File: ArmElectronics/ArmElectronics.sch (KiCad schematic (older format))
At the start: 90 parts, among them J1 Raspberry_Pi_2_3, J10 AH1815 Breakout, J11 AH1815 Breakout, J12 AH1815 Breakout, J13 AH1815 Breakout, J14 AH1815 Breakout, J15 AH1815 Breakout, J16 AH1815 Breakout, J17 AH1815 Breakout, J18 AH1815 Breakout, J19 AH1815 Breakout, J2 12V In, J20 AH1815 Breakout, J21 AH1815 Breakout, J3 RasPi Power Out, J4 Batt In, J5 Batt Out, J6 BNO055 QWIIC Conn, J7 Conn_01x14, J8 Encoder Breakout, J9 1792245, U1 Teensy4.1, U10 PA-09, U11 74LVC1G97, U12 74LVC1G97, U13 74LVC1G97, U14 74LVC1G97, U15 74LVC1G97, U16 74LVC1G97, U18 MAX11601, U2 Pololu_2857, U3 Pololu_2851, U4 Pololu_3730, U5 TB9051FTG, U6 TB9051FTG, U7 TB9051FTG, U8 PA-09, U9 PA-09

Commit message: reannotated schematic
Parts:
- renumbered C7 to C1, C1 to C2, C2 to C3, C3 to C4, C4 to C5, C5 to C6, C6 to C7, J18 to J17, J19 to J18, J20 to J19, J7 to J2, J21 to J20, J9 to J21, J8 to J3, J3 to J4, J2 to J5, J4 to J6, J5 to J7, J6 to J8, J17 to J9, R31 to R1, R40 to R10, R41 to R11, R25 to R12, R26 to R13, R4 to R14, R5 to R15, R6 to R16, R10 to R17, R11 to R18, R12 to R19, R32 to R2, R1 to R20, R2 to R21, R27 to R22, R28 to R23, R3 to R24, R7 to R25, R13 to R26, R14 to R27, R15 to R28, R16 to R29, R33 to R3, R17 to R30, R18 to R31, R29 to R32, R30 to R33, R8 to R34, R9 to R35, R19 to R36, R20 to R37, R21 to R38, R22 to R39, R34 to R4, R23 to R40, R24 to R41, R35 to R5, R36 to R6, R38 to R7, R39 to R8, R37 to R9, U9 to U10, U10 to U11, U11 to U12, U12 to U13, U13 to U14, U14 to U15, U15 to U16, U16 to U17, U18 to U3, U3 to U4, U4 to U5, U5 to U6, U6 to U7, U7 to U8, U8 to U9
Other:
- moved on the sheet: J10, J11, J12, J13, J14, J15, J16, J17, J18, J19, J20, J9

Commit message: forgot to hit save in eeschema
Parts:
- renumbered U9 to J22, U10 to J23, U11 to J24
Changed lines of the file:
@@
 $EndComp
 $Comp
-L ArmElectronics_Library:PA-09 U9
+L ArmElectronics_Library:PA-09 J22
 U 1 1 5F84EEEA
 P 14200 1400
-F 0 "U9" H 14500 1915 50  0000 C CNN
+F 0 "J22" H 14500 1915 50  0000 C CNN
 F 1 "PA-09" H 14500 1824 50  0000 C CNN
 F 2 "Connector_Molex:Molex_Mini-Fit_Jr_5566-06A_2x03_P4.20mm_Vertical" H 14500 1250 50  0001 C CNN
@@
 M1_HALL2
 $Comp
-L ArmElectronics_Library:PA-09 U10
+L ArmElectronics_Library:PA-09 J23
 U 1 1 5F871CC2
 P 14200 3050
-F 0 "U10" H 14500 3565 50  0000 C CNN
+F 0 "J23" H 14500 3565 50  0000 C CNN
 F 1 "PA-09" H 14500 3474 50  0000 C CNN
 F 2 "Connector_Molex:Molex_Mini-Fit_Jr_5566-06A_2x03_P4.20mm_Vertical" H 14500 2900 50  0001 C CNN
@@
 	15050 2800 15150 2800
 $Comp
-L ArmElectronics_Library:PA-09 U11
+L ArmElectronics_Library:PA-09 J24
 U 1 1 5F878EF2
 P 14200 4650
-F 0 "U11" H 14500 5165 50  0000 C CNN
+F 0 "J24" H 14500 5165 50  0000 C CNN
 F 1 "PA-09" H 14500 5074 50  0000 C CNN
 F 2 "Connector_Molex:Molex_Mini-Fit_Jr_5566-06A_2x03_P4.20mm_Vertical" H 14500 4500 50  0001 C CNN

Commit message: Please be done now
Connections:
- net Hall_SW_1: now also U1.36 (P29); no longer U1.4 (P2)
- net Hall_SW_10: now also U1.7 (P5); no longer U1.38 (P31)
- net Hall_SW_11: now also U1.4 (P2); no longer U1.39 (P32)
- net Hall_SW_12: now also U1.5 (P3); no longer U1.40 (P33)
- net Hall_SW_2: now also U1.40 (P33); no longer U1.5 (P3)
- net Hall_SW_3: now also U1.35 (P28); no longer U1.6 (P4)
- net Hall_SW_4: now also U1.34 (P27); no longer U1.7 (P5)
- net Hall_SW_5: now also U1.39 (P32); no longer U1.8 (P6)
- net Hall_SW_6: now also U1.37 (P30); no longer U1.32 (P25)
- net Hall_SW_7: now also U1.8 (P6); no longer U1.35 (P28)
- net Hall_SW_8: now also U1.38 (P31); no longer U1.36 (P29)
- net Hall_SW_9: now also U1.6 (P4); no longer U1.37 (P30)
- net Stepper_BEMF: now also U1.33 (P26); no longer U1.34 (P27)
- net Stepper_Stall: now also U1.32 (P25); no longer U1.33 (P26)
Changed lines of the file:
@@
 Text Label 4600 2200 2    50   ~ 0
 Stepper_Fault
+Text Label 4600 3000 2    50   ~ 0
+Stepper_Stall
 Text Label 4600 3100 2    50   ~ 0
-Stepper_Stall
-Text Label 4600 3200 2    50   ~ 0
 Stepper_BEMF
 $Comp
@@
 Text Label 9050 14600 0    50   ~ 0
 Hall_SW_6
-Text Label 4600 3000 2    50   ~ 0
+Text Label 4600 3500 2    50   ~ 0
 Hall_SW_6
+Text Label 4600 3700 2    50   ~ 0
+Hall_SW_5
+Text Label 4600 3300 2    50   ~ 0
+Hall_SW_3
+Text Label 5400 3700 0    50   ~ 0
+Hall_SW_2
+Text Label 4600 3400 2    50   ~ 0
+Hall_SW_1
 Text Label 4600 2100 2    50   ~ 0
-Hall_SW_5
-Text Label 4600 2000 2    50   ~ 0
-Hall_SW_4
+Hall_SW_7
+Text Label 4600 3600 2    50   ~ 0
+Hall_SW_8
 Text Label 4600 1900 2    50   ~ 0
-Hall_SW_3
-Text Label 4600 1800 2    50   ~ 0
-Hall_SW_2
-Text Label 4600 1700 2    50   ~ 0
-Hall_SW_1
-Text Label 4600 3300 2    50   ~ 0
-Hall_SW_7
-Text Label 4600 3400 2    50   ~ 0
-Hall_SW_8
-Text Label 4600 3500 2    50   ~ 0
 Hall_SW_9
-Text Label 4600 3600 2    50   ~ 0
-Hall_SW_10
-Text Label 4600 3700 2    50   ~ 0
-Hall_SW_11
-Text Label 5400 3700 0    50   ~ 0
-Hall_SW_12
 $Comp
 L ArmElectronics_Library:TB9051FTG U6
@@
 	1    0    0    -1
 $EndComp
+Text Label 4600 2000 2    50   ~ 0
+Hall_SW_10
+Text Label 4600 1700 2    50   ~ 0
+Hall_SW_11
+Text Label 4600 1800 2    50   ~ 0
+Hall_SW_12
+Text Label 4600 3200 2    50   ~ 0
+Hall_SW_4
 $EndSCHEMATC

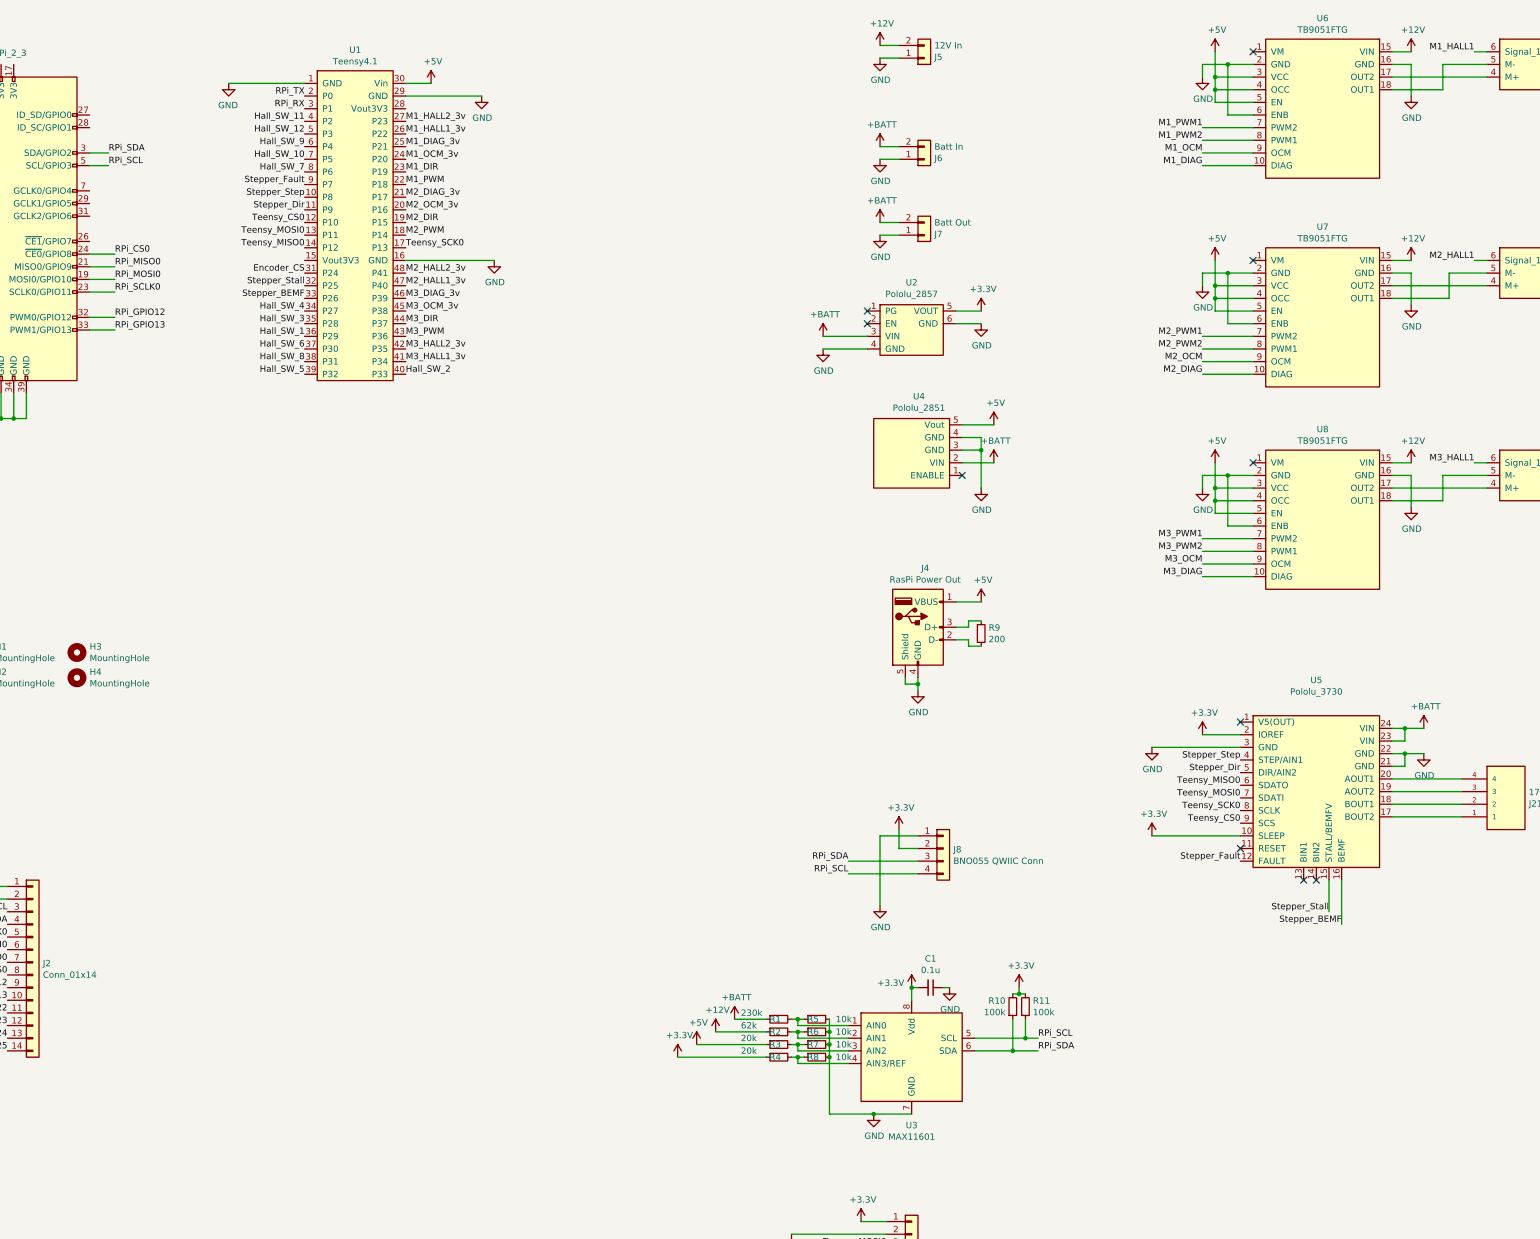
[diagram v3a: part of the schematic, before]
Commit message: Added an E-Stop switch and motor off function
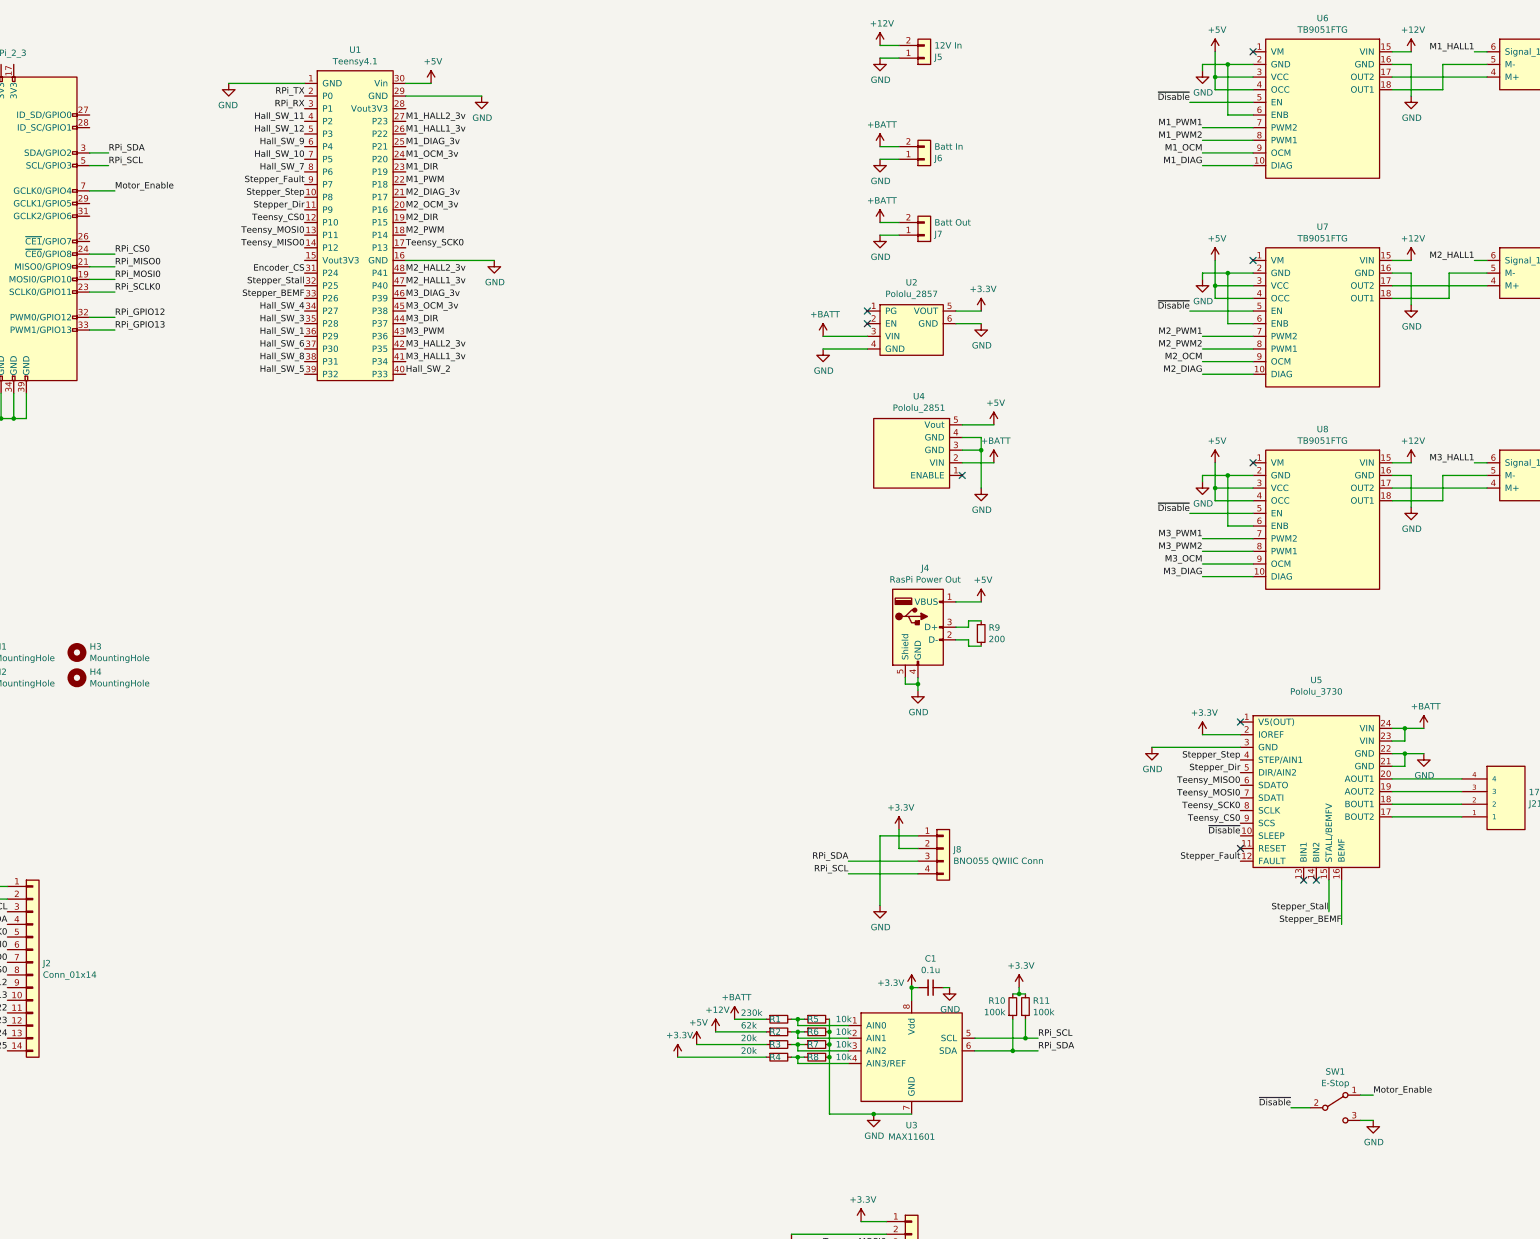
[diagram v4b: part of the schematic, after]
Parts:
- added SW1: E-Stop, Connector_JST:JST_PH_B3B-PH-K_1x03_P2.00mm_Vertical, symbol Switch:SW_SPDT
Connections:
- net +3V3: no longer U5.10 (SLEEP)
- net +5V: no longer U6.5 (EN), U7.5 (EN), U8.5 (EN)
- net GND: now also SW1.3 (C)
- net Motor_Enable: now reaches J1.7 (GCLK0/GPIO4)
- net Motor_Enable: now also SW1.1 (A)
- new net ~Disable: SW1.2 (B), U5.10 (SLEEP), U6.5 (EN), U7.5 (EN), U8.5 (EN)
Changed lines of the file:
@@
 Wire Wire Line
 	13350 1500 13350 1250
-$Comp
-L power:GND #PWR061
-U 1 1 5F859BFE
-P 11700 1350
-F 0 "#PWR061" H 11700 1100 50  0001 C CNN
-F 1 "GND" H 11705 1177 50  0000 C CNN
-F 2 "" H 11700 1350 50  0001 C CNN
-F 3 "" H 11700 1350 50  0001 C CNN
-	1    11700 1350
-	1    0    0    -1
-$EndComp
-Wire Wire Line
-	11700 1350 11700 1250
-Wire Wire Line
-	11700 1250 11900 1250
-$Comp
-L power:+5V #PWR065
-U 1 1 5F85A73B
-P 11800 1150
-F 0 "#PWR065" H 11800 1000 50  0001 C CNN
-F 1 "+5V" H 11815 1323 50  0000 C CNN
-F 2 "" H 11800 1150 50  0001 C CNN
-F 3 "" H 11800 1150 50  0001 C CNN
-	1    11800 1150
-	1    0    0    -1
-$EndComp
-Wire Wire Line
-	11800 1150 11800 1350
-Wire Wire Line
-	11800 1350 12100 1350
-Wire Wire Line
-	11800 1350 11800 1450
-Wire Wire Line
-	11800 1550 12100 1550
-Connection ~ 11800 1350
-Wire Wire Line
-	12100 1650 11900 1650
-Wire Wire Line
-	11900 1650 11900 1250
-Connection ~ 11900 1250
-Wire Wire Line
-	11900 1250 12100 1250
-Wire Wire Line
-	12100 1450 11800 1450
-Connection ~ 11800 1450
-Wire Wire Line
-	11800 1450 11800 1550
 NoConn ~ 12100 1150
 Text Label 11700 1750 2    50   ~ 0
@@
 Wire Wire Line
 	13350 3150 13350 2900
-$Comp
-L power:GND #PWR062
-U 1 1 5F871CF3
-P 11700 3000
-F 0 "#PWR062" H 11700 2750 50  0001 C CNN
-F 1 "GND" H 11705 2827 50  0000 C CNN
-F 2 "" H 11700 3000 50  0001 C CNN
-F 3 "" H 11700 3000 50  0001 C CNN
-	1    11700 3000
-	1    0    0    -1
-$EndComp
-Wire Wire Line
-	11700 3000 11700 2900
-Wire Wire Line
-	11700 2900 11900 2900
-$Comp
-L power:+5V #PWR066
-U 1 1 5F871CFF
-P 11800 2800
-F 0 "#PWR066" H 11800 2650 50  0001 C CNN
-F 1 "+5V" H 11815 2973 50  0000 C CNN
-F 2 "" H 11800 2800 50  0001 C CNN
-F 3 "" H 11800 2800 50  0001 C CNN
-	1    11800 2800
-	1    0    0    -1
-$EndComp
-Wire Wire Line
-	11800 2800 11800 3000
-Wire Wire Line
-	11800 3000 12100 3000
-Wire Wire Line
-	11800 3000 11800 3100
-Wire Wire Line
-	11800 3200 12100 3200
-Connection ~ 11800 3000
-Wire Wire Line
-	12100 3300 11900 3300
-Wire Wire Line
-	11900 3300 11900 2900
-Connection ~ 11900 2900
-Wire Wire Line
-	11900 2900 12100 2900
-Wire Wire Line
-	12100 3100 11800 3100
-Connection ~ 11800 3100
-Wire Wire Line
-	11800 3100 11800 3200
 NoConn ~ 12100 2800
 Text Label 11700 3400 2    50   ~ 0
@@
 L power:GND #PWR063
 U 1 1 5F878F23
-P 11700 4600
-F 0 "#PWR063" H 11700 4350 50  0001 C CNN
-F 1 "GND" H 11705 4427 50  0000 C CNN
-F 2 "" H 11700 4600 50  0001 C CNN
-F 3 "" H 11700 4600 50  0001 C CNN
-	1    11700 4600
+P 11700 4550
+F 0 "#PWR063" H 11700 4300 50  0001 C CNN
+F 1 "GND" H 11705 4377 50  0000 C CNN
+F 2 "" H 11700 4550 50  0001 C CNN
+F 3 "" H 11700 4550 50  0001 C CNN
+	1    11700 4550
 	1    0    0    -1
 $EndComp
 Wire Wire Line
-	11700 4600 11700 4500
+	11700 4550 11700 4500
 Wire Wire Line
 	11700 4500 11900 4500
@@
 Wire Wire Line
 	11800 4600 11800 4700
-Wire Wire Line
-	11800 4800 12100 4800
 Connection ~ 11800 4600
 Wire Wire Line
@@
 Wire Wire Line
 	12100 4700 11800 4700
-Connection ~ 11800 4700
-Wire Wire Line
-	11800 4700 11800 4800
 NoConn ~ 12100 4400
 Text Label 11700 5000 2    50   ~ 0
@@
 NoConn ~ 12000 6450
 $Comp
-L power:+3.3V #PWR060
-U 1 1 5FD65C7A
-P 11300 7350
-F 0 "#PWR060" H 11300 7200 50  0001 C CNN
-F 1 "+3.3V" H 11315 7523 50  0000 C CNN
-F 2 "" H 11300 7350 50  0001 C CNN
-F 3 "" H 11300 7350 50  0001 C CNN
-	1    11300 7350
-	1    0    0    -1
-$EndComp
-Wire Wire Line
-	11300 7350 12000 7350
-$Comp
 L power:GND #PWR059
 U 1 1 5FDA6F4C
@@
 Text Label 4600 3200 2    50   ~ 0
 Hall_SW_4
+Text Label 12000 7350 2    50   ~ 0
+~Disable
+Text Label 11600 4800 2    50   ~ 0
+~Disable
+Wire Wire Line
+	11600 4800 12100 4800
+$Comp
+L power:GND #PWR0121
+U 1 1 60E5F442
+P 11700 2950
+F 0 "#PWR0121" H 11700 2700 50  0001 C CNN
+F 1 "GND" H 11705 2777 50  0000 C CNN
+F 2 "" H 11700 2950 50  0001 C CNN
+F 3 "" H 11700 2950 50  0001 C CNN
+	1    11700 2950
+	1    0    0    -1
+$EndComp
+Wire Wire Line
+	11700 2950 11700 2900
+Wire Wire Line
+	11700 2900 11900 2900
+$Comp
+L power:+5V #PWR0122
+U 1 1 60E5F44A
+P 11800 2800
+F 0 "#PWR0122" H 11800 2650 50  0001 C CNN
+F 1 "+5V" H 11815 2973 50  0000 C CNN
+F 2 "" H 11800 2800 50  0001 C CNN
+F 3 "" H 11800 2800 50  0001 C CNN
+	1    11800 2800
+	1    0    0    -1
+$EndComp
+Wire Wire Line
+	11800 2800 11800 3000
+Wire Wire Line
+	11800 3000 12100 3000
+Wire Wire Line
+	11800 3000 11800 3100
+Connection ~ 11800 3000
+Wire Wire Line
+	12100 3300 11900 3300
+Wire Wire Line
+	11900 3300 11900 2900
+Connection ~ 11900 2900
+Wire Wire Line
+	11900 2900 12100 2900
+Wire Wire Line
+	12100 3100 11800 3100
+Text Label 11600 3200 2    50   ~ 0
+~Disable
+Wire Wire Line
+	11600 3200 12100 3200
+$Comp
+L power:GND #PWR0123
+U 1 1 60E9F3A7
+P 11700 1300
+F 0 "#PWR0123" H 11700 1050 50  0001 C CNN
+F 1 "GND" H 11705 1127 50  0000 C CNN
+F 2 "" H 11700 1300 50  0001 C CNN
+F 3 "" H 11700 1300 50  0001 C CNN
+	1    11700 1300
+	1    0    0    -1
+$EndComp
+Wire Wire Line
+	11700 1300 11700 1250
+Wire Wire Line
+	11700 1250 11900 1250
+$Comp
+L power:+5V #PWR0124
+U 1 1 60E9F3AF
+P 11800 1150
+F 0 "#PWR0124" H 11800 1000 50  0001 C CNN
+F 1 "+5V" H 11815 1323 50  0000 C CNN
+F 2 "" H 11800 1150 50  0001 C CNN
+F 3 "" H 11800 1150 50  0001 C CNN
+	1    11800 1150
+	1    0    0    -1
+$EndComp
+Wire Wire Line
+	11800 1150 11800 1350
+Wire Wire Line
+	11800 1350 12100 1350
+Wire Wire Line
+	11800 1350 11800 1450
+Connection ~ 11800 1350
+Wire Wire Line
+	12100 1650 11900 1650
+Wire Wire Line
+	11900 1650 11900 1250
+Connection ~ 11900 1250
+Wire Wire Line
+	11900 1250 12100 1250
+Wire Wire Line
+	12100 1450 11800 1450
+Text Label 11600 1550 2    50   ~ 0
+~Disable
+Wire Wire Line
+	11600 1550 12100 1550
+Text Label 12400 9500 2    50   ~ 0
+~Disable
+$Comp
+L Switch:SW_SPDT SW1
+U 1 1 60EC33BA
+P 12750 9500
+F 0 "SW1" H 12750 9785 50  0000 C CNN
+F 1 "E-Stop" H 12750 9694 50  0000 C CNN
+F 2 "Connector_JST:JST_PH_B3B-PH-K_1x03_P2.00mm_Vertical" H 12750 9500 50  0001 C CNN
+F 3 "~" H 12750 9500 50  0001 C CNN
+	1    12750 9500
+	1    0    0    -1
+$EndComp
+Wire Wire Line
+	12400 9500 12550 9500
+$Comp
+L power:GND #PWR0125
+U 1 1 60EE9EE2
+P 13050 9600
+F 0 "#PWR0125" H 13050 9350 50  0001 C CNN
+F 1 "GND" H 13055 9427 50  0000 C CNN
+F 2 "" H 13050 9600 50  0001 C CNN
+F 3 "" H 13050 9600 50  0001 C CNN
+	1    13050 9600
+	1    0    0    -1
+$EndComp
+Wire Wire Line
+	13050 9600 12950 9600
+Text Label 13050 9400 0    50   ~ 0
+Motor_Enable
+Wire Wire Line
+	13050 9400 12950 9400
+Text Label 3100 2250 0    50   ~ 0
+Motor_Enable
+Wire Wire Line
+	3100 2250 2900 2250
 $EndSCHEMATC
